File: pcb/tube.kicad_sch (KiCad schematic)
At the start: 80 parts, among them J1 Screw_Terminal_01x02, J10 LED_[5..8], J11 LED_[1..4], J2 Screw_Terminal_01x02, J3 Screw_Terminal_01x02, J4 Conn_01x04_Pin, J5 Conn_01x08_Pin, J6 Conn_01x05_Pin, U1 INA226, U10 74LS32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

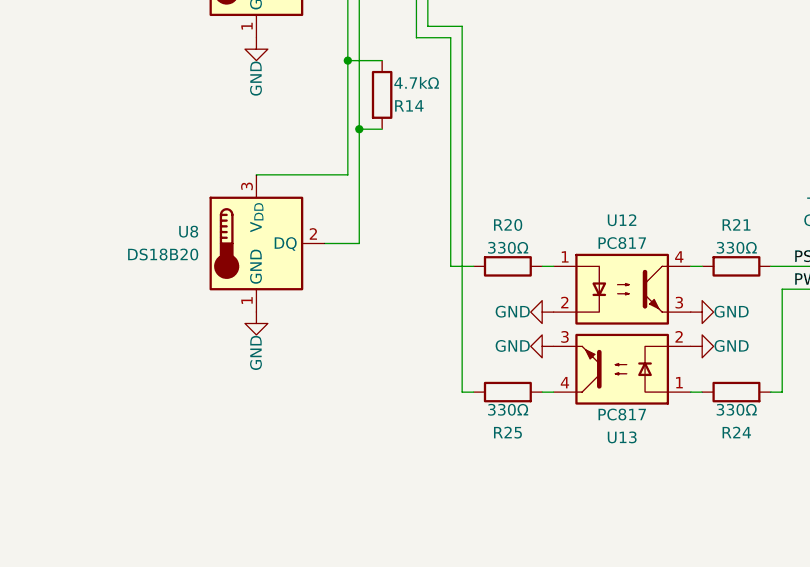
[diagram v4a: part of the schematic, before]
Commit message: PCB: Add 10k PWGood Pullup
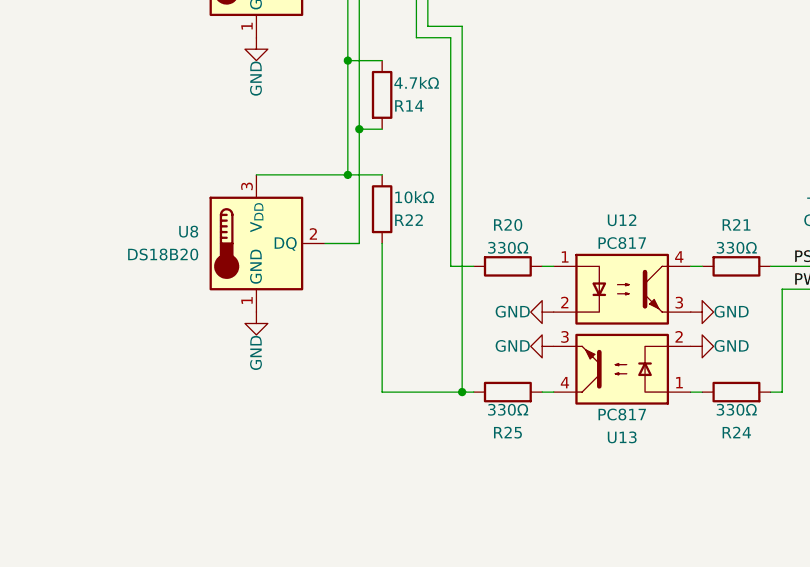
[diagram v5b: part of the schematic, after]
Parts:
- added R22: 10kΩ, Resistor_SMD:R_0805_2012Metric, symbol Device:R
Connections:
- net +3.3V1: now also R22.1
- net at R25.1, U4.21 (29_TX7): now also R22.2
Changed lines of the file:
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@@
   (junction (at 46.99 83.82) (diameter 0) (color 0 0 0 0)
   )
+  (junction (at 209.55 203.2) (diameter 0) (color 0 0 0 0)
+  )
   (junction (at 115.57 40.64) (diameter 0) (color 0 0 0 0)
   )
   (junction (at 180.34 22.86) (diameter 0) (color 0 0 0 0)
+  )
+  (junction (at 196.85 179.07) (diameter 0) (color 0 0 0 0)
   )
   (junction (at 274.32 156.21) (diameter 0) (color 0 0 0 0)
@@
     (stroke (width 0) (type default))
   )
+  (wire (pts (xy 200.66 186.69) (xy 200.66 203.2))
+    (stroke (width 0) (type default))
+  )
   (wire (pts (xy 194.31 186.69) (xy 198.12 186.69))
     (stroke (width 0) (type default))
@@
     (stroke (width 0) (type default))
   )
+  (wire (pts (xy 200.66 203.2) (xy 209.55 203.2))
+    (stroke (width 0) (type default))
+  )
   (bus (pts (xy 195.58 90.17) (xy 195.58 92.71))
     (stroke (width 0) (type default))
@@
   )
   (bus (pts (xy 153.67 119.38) (xy 153.67 121.92))
+    (stroke (width 0) (type default))
+  )
+  (wire (pts (xy 196.85 179.07) (xy 200.66 179.07))
     (stroke (width 0) (type default))
   )
@@
         )
       )
+    )
+  )
+  (symbol (lib_id "Device:R") (at 200.66 182.88 0) (unit 1)
+    (in_bom yes) (on_board yes) (dnp no)
+    (property "Reference" "R22" (at 201.93 184.15 0)
+      (effects (font (size 1.27 1.27)) (justify left))
+    )
+    (property "Value" "10kΩ" (at 201.93 181.61 0)
+      (effects (font (size 1.27 1.27)) (justify left))
+    )
+    (property "Footprint" "Resistor_SMD:R_0805_2012Metric" (at 198.882 182.88 90)
+      (effects (font (size 1.27 1.27)) hide)
+    )
+    (property "Datasheet" "~" (at 200.66 182.88 0)
+      (effects (font (size 1.27 1.27)) hide)
+    )
+    (pin "2")
+    (pin "1")
+    (instances
+      (project "tube"
+        (path "/17a681e7-f555-4501-b0f6-333651e2bfd6"
+          (reference "R22") (unit 1)
+        )
+      )

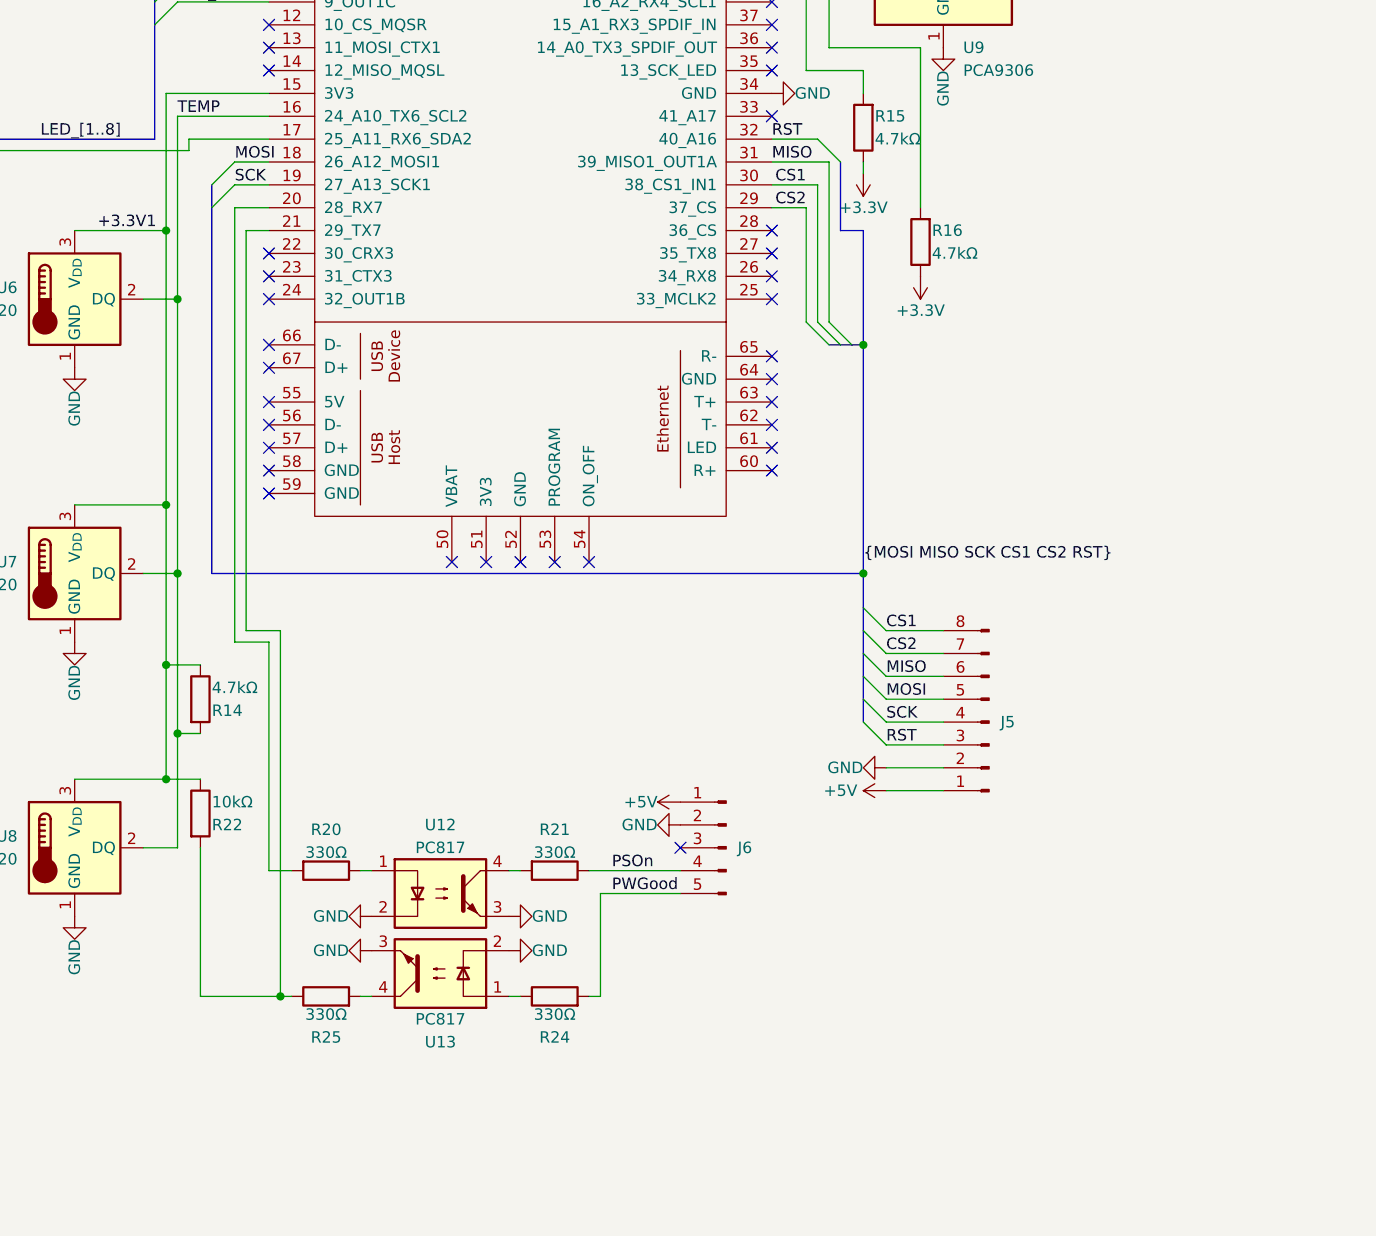
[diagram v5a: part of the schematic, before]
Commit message: PCB: Add SPI Voltage Shift
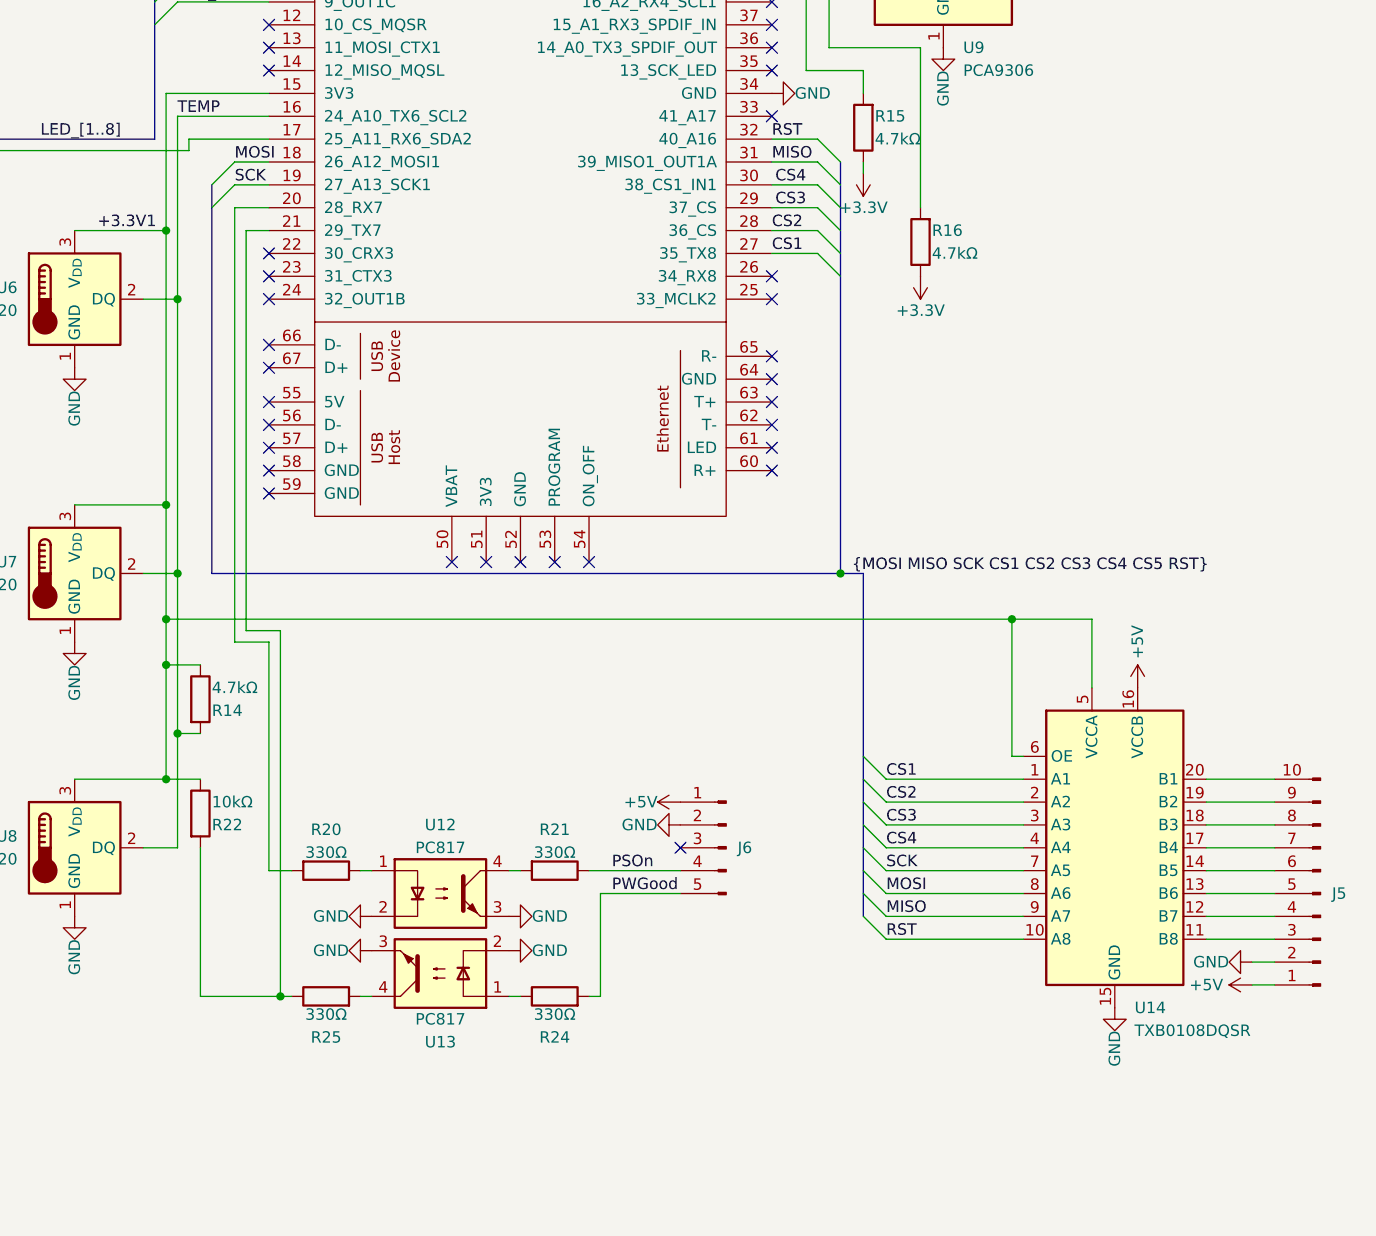
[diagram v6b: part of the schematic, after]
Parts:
- removed J5: Conn_01x08_Pin, Connector_PinHeader_2.54mm:PinHeader_1x08_P2.54mm_Vertical, symbol Connector:Conn_01x08_Pin
- added J5: Conn_01x10_Pin, Connector_PinHeader_2.54mm:PinHeader_1x10_P2.54mm_Vertical, symbol Connector:Conn_01x10_Pin
- added U14: TXB0108DQSR, Package_SO:HTSSOP-20-1EP_4.4x6.5mm_P0.65mm_EP2.74x3.86mm, symbol Logic_LevelTranslator:TXB0108DQSR
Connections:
- net +3.3V1: now also U14.5 (VCCA), U14.6 (OE)
- net +5V: now also J5.1 (Pin_1), U14.16 (VCCB)
- net CS1: now also U4.27 (35_TX8), U14.1 (A1); no longer U4.30 (38_CS1_IN1)
- net CS2: now also U4.28 (36_CS), U14.2 (A2); no longer U4.29 (37_CS)
- net GND: now also J5.2 (Pin_2), U14.15 (GND)
- net MISO: now also U14.9 (A7)
- net MOSI: now also U14.8 (A6)
- net RST: now also U14.10 (A8)
- net SCK: now also U14.7 (A5)
- new net: J5.3 (Pin_3), U14.11 (B8)
- new net: J5.4 (Pin_4), U14.12 (B7)
- new net: J5.5 (Pin_5), U14.13 (B6)
- new net: J5.6 (Pin_6), U14.14 (B5)
- new net: J5.7 (Pin_7), U14.17 (B4)
- new net: J5.8 (Pin_8), U14.18 (B3)
- new net: J5.9 (Pin_9), U14.19 (B2)
- new net: J5.10 (Pin_10), U14.20 (B1)
- new net CS3: U14.3 (A3), U4.29 (37_CS)
- new net CS4: U14.4 (A4), U4.30 (38_CS1_IN1)
- no-connect marks 47 -> 45

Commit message: PCB: Optimize Traces
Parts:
- J5: footprint Connector_PinHeader_2.54mm:PinHeader_1x10_P2.54mm_Vertical -> Connector_PinHeader_2.54mm:PinHeader_1x10_P2.54mm_Horizontal
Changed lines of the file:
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@@
       (effects (font (size 1.27 1.27)) (justify right) hide)
     )
-    (property "Footprint" "Connector_PinHeader_2.54mm:PinHeader_1x10_P2.54mm_Vertical" (at 325.12 191.77 0)
+    (property "Footprint" "Connector_PinHeader_2.54mm:PinHeader_1x10_P2.54mm_Horizontal" (at 325.12 191.77 0)
       (effects (font (size 1.27 1.27)) hide)
     )

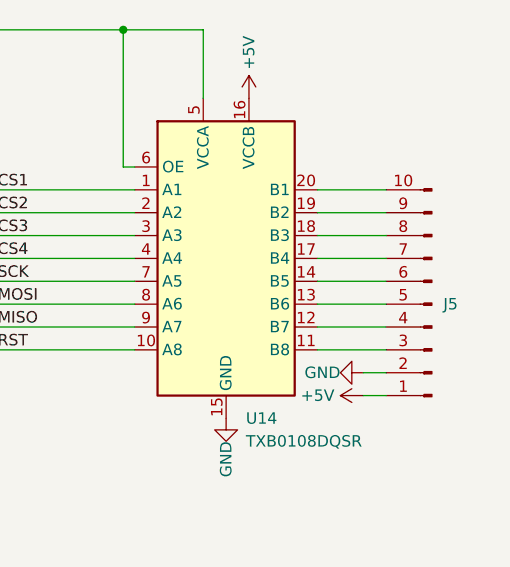
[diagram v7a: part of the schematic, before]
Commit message: PCB: Add SPI Silkscreen
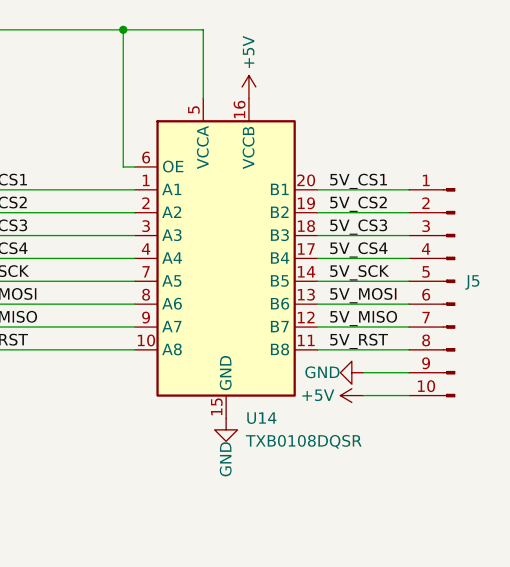
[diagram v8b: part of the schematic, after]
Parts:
- J5: footprint Connector_PinHeader_2.54mm:PinHeader_1x10_P2.54mm_Horizontal -> Connector_PinHeader_2.54mm:PinHeader_1x10_P2.54mm_Vertical
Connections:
- net +5V: now also J5.10 (Pin_10); no longer J5.1 (Pin_1)
- net GND: now also J5.9 (Pin_9); no longer J5.2 (Pin_2)
- net 5V_CS3: now reaches J5.3 (Pin_3)
- net 5V_CS3: now also U14.18 (B3); no longer U14.11 (B8)
- net 5V_CS4: now reaches J5.4 (Pin_4)
- net 5V_CS4: now also U14.17 (B4); no longer U14.12 (B7)
- net 5V_MOSI: now reaches U14.13 (B6)
- net 5V_MOSI: now also J5.6 (Pin_6); no longer J5.5 (Pin_5)
- net 5V_SCK: now reaches U14.14 (B5)
- net 5V_SCK: now also J5.5 (Pin_5); no longer J5.6 (Pin_6)
- net 5V_MISO: now reaches J5.7 (Pin_7)
- net 5V_MISO: now also U14.12 (B7); no longer U14.17 (B4)
- net 5V_RST: now reaches J5.8 (Pin_8)
- net 5V_RST: now also U14.11 (B8); no longer U14.18 (B3)
- net 5V_CS2: now reaches U14.19 (B2)
- net 5V_CS2: now also J5.2 (Pin_2); no longer J5.9 (Pin_9)
- net 5V_CS1: now reaches U14.20 (B1)
- net 5V_CS1: now also J5.1 (Pin_1); no longer J5.10 (Pin_10)
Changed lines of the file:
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@@
     (stroke (width 0) (type default))
   )
-  (wire (pts (xy 320.04 181.61) (xy 312.42 181.61))
+  (wire (pts (xy 322.58 181.61) (xy 312.42 181.61))
     (stroke (width 0) (type default))
   )
@@
     (stroke (width 0) (type default))
   )
-  (wire (pts (xy 320.04 184.15) (xy 312.42 184.15))
+  (wire (pts (xy 322.58 184.15) (xy 312.42 184.15))
     (stroke (width 0) (type default))
   )
@@
     (stroke (width 0) (type default))
   )
-  (wire (pts (xy 320.04 189.23) (xy 312.42 189.23))
+  (wire (pts (xy 322.58 189.23) (xy 312.42 189.23))
     (stroke (width 0) (type default))
   )
@@
     (stroke (width 0) (type default))
   )
-  (wire (pts (xy 317.5 201.93) (xy 320.04 201.93))
+  (wire (pts (xy 317.5 201.93) (xy 322.58 201.93))
     (stroke (width 0) (type default))
   )
@@
     (stroke (width 0) (type default))
   )
-  (wire (pts (xy 320.04 186.69) (xy 312.42 186.69))
+  (wire (pts (xy 322.58 186.69) (xy 312.42 186.69))
     (stroke (width 0) (type default))
   )
@@
     (stroke (width 0) (type default))
   )
-  (wire (pts (xy 320.04 194.31) (xy 312.42 194.31))
+  (wire (pts (xy 322.58 194.31) (xy 312.42 194.31))
     (stroke (width 0) (type default))
   )
@@
     (stroke (width 0) (type default))
   )
-  (wire (pts (xy 317.5 199.39) (xy 320.04 199.39))
+  (wire (pts (xy 317.5 199.39) (xy 322.58 199.39))
     (stroke (width 0) (type default))
   )
@@
     (stroke (width 0) (type default))
   )
-  (wire (pts (xy 320.04 196.85) (xy 312.42 196.85))
+  (wire (pts (xy 322.58 196.85) (xy 312.42 196.85))
     (stroke (width 0) (type default))
   )
@@
     (stroke (width 0) (type default))
   )
-  (wire (pts (xy 320.04 191.77) (xy 312.42 191.77))
+  (wire (pts (xy 322.58 191.77) (xy 312.42 191.77))
     (stroke (width 0) (type default))
   )
@@
     (stroke (width 0) (type default))
   )
-  (wire (pts (xy 320.04 179.07) (xy 312.42 179.07))
+  (wire (pts (xy 322.58 179.07) (xy 312.42 179.07))
     (stroke (width 0) (type default))
   )
@@
     (effects (font (size 1.27 1.27)) (justify right bottom))
   )
+  (label "5V_CS2" (at 313.69 181.61 0) (fields_autoplaced)
+    (effects (font (size 1.27 1.27)) (justify left bottom))
+  )
   (label "I3_A0" (at 128.27 80.01 90) (fields_autoplaced)
     (effects (font (size 1.27 1.27)) (justify left bottom))
@@
     (effects (font (size 1.27 1.27)) (justify left bottom))
   )
+  (label "5V_MOSI" (at 313.69 191.77 0) (fields_autoplaced)
+    (effects (font (size 1.27 1.27)) (justify left bottom))
+  )
   (label "Vin2-" (at 72.39 36.83 180) (fields_autoplaced)
     (effects (font (size 1.27 1.27)) (justify right bottom))
@@
     (effects (font (size 1.27 1.27)) (justify left bottom))
   )
+  (label "5V_CS4" (at 313.69 186.69 0) (fields_autoplaced)
+    (effects (font (size 1.27 1.27)) (justify left bottom))
+  )
   (label "SCL" (at 69.85 81.28 0) (fields_autoplaced)
     (effects (font (size 1.27 1.27)) (justify left bottom))
@@
     (effects (font (size 1.27 1.27)) (justify left bottom))
   )
+  (label "5V_MISO" (at 313.69 194.31 0) (fields_autoplaced)
+    (effects (font (size 1.27 1.27)) (justify left bottom))
+  )
   (label "SCL" (at 203.2 49.53 0) (fields_autoplaced)
     (effects (font (size 1.27 1.27)) (justify left bottom))
@@
     (effects (font (size 1.27 1.27)) (justify left bottom))
   )
+  (label "5V_SCK" (at 313.69 189.23 0) (fields_autoplaced)
+    (effects (font (size 1.27 1.27)) (justify left bottom))
+  )
   (label "SDA" (at 113.1011 78.74 0) (fields_autoplaced)
     (effects (font (size 1.27 1.27)) (justify left bottom))
@@
     (effects (font (size 1.27 1.27)) (justify right bottom))
   )
+  (label "5V_CS3" (at 313.69 184.15 0) (fields_autoplaced)
+    (effects (font (size 1.27 1.27)) (justify left bottom))
+  )
   (label "LED_6" (at 151.13 124.46 180) (fields_autoplaced)
     (effects (font (size 1.27 1.27)) (justify right bottom))
@@
     (effects (font (size 1.27 1.27)) (justify left bottom))
   )
+  (label "5V_RST" (at 313.69 196.85 0) (fields_autoplaced)
+    (effects (font (size 1.27 1.27)) (justify left bottom))
+  )
   (label "LED_5" (at 151.13 127 180) (fields_autoplaced)
     (effects (font (size 1.27 1.27)) (justify right bottom))
@@
     (effects (font (size 1.27 1.27)) (justify left bottom))
   )
+  (label "5V_CS1" (at 313.69 179.07 0) (fields_autoplaced)
+    (effects (font (size 1.27 1.27)) (justify left bottom))
+  )
   (label "+3.3V1" (at 189.23 118.11 0) (fields_autoplaced)
     (effects (font (size 1.27 1.27)) (justify left bottom))
@@
     )
   )
-  (symbol (lib_id "Connector:Conn_01x10_Pin") (at 325.12 191.77 180) (unit 1)
-    (in_bom yes) (on_board yes) (dnp no)
-    (property "Reference" "J5" (at 326.39 191.77 0)
-      (effects (font (size 1.27 1.27)) (justify right))
-    )
-    (property "Value" "Conn_01x10_Pin" (at 326.39 191.77 0)
-      (effects (font (size 1.27 1.27)) (justify right) hide)
-    )
-    (property "Footprint" "Connector_PinHeader_2.54mm:PinHeader_1x10_P2.54mm_Horizontal" (at 325.12 191.77 0)
-      (effects (font (size 1.27 1.27)) hide)
-    )
-    (property "Datasheet" "~" (at 325.12 191.77 0)
-      (effects (font (size 1.27 1.27)) hide)
-    )
-    (pin "2")
-    (pin "8")
-    (pin "4")
-    (pin "6")
-    (pin "5")
-    (pin "7")
-    (pin "3")
-    (pin "1")
-    (pin "9")
-    (pin "10")
-    (instances
-      (project "tube"
-        (path "/17a681e7-f555-4501-b0f6-333651e2bfd6"
-          (reference "J5") (unit 1)
-        )
-      )
-    )
-  )
   (symbol (lib_id "power:+5V") (at 293.37 82.55 270) (unit 1)
     (in_bom yes) (on_board yes) (dnp no)
@@
         )
       )
+    )
+  )
+  (symbol (lib_id "Connector:Conn_01x10_Pin") (at 327.66 189.23 0) (mirror y) (unit 1)
+    (in_bom yes) (on_board yes) (dnp no)
+    (property "Reference" "J5" (at 328.93 189.23 0)
+      (effects (font (size 1.27 1.27)) (justify right))
+    )
+    (property "Value" "Conn_01x10_Pin" (at 328.93 189.23 0)
+      (effects (font (size 1.27 1.27)) (justify right) hide)
+    )
+    (property "Footprint" "Connector_PinHeader_2.54mm:PinHeader_1x10_P2.54mm_Vertical" (at 327.66 189.23 0)
+      (effects (font (size 1.27 1.27)) hide)
+    )
+    (property "Datasheet" "~" (at 327.66 189.23 0)
+      (effects (font (size 1.27 1.27)) hide)
+    )
+    (pin "2")
+    (pin "8")
+    (pin "4")
+    (pin "6")
+    (pin "5")
+    (pin "7")
+    (pin "3")
+    (pin "1")
+    (pin "9")
+    (pin "10")
+    (instances
+      (project "tube"
+        (path "/17a681e7-f555-4501-b0f6-333651e2bfd6"
+          (reference "J5") (unit 1)
+        )
+      )
